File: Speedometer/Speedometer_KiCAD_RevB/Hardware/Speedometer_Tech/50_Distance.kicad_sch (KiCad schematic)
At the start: 30 parts, among them U510 TLC59108IPWR, U511 TLC59108IPWR, U512 TLC59108IPWR, U513 TLC59108IPWR, U514 TLC59108IPWR, U515 TLC59108IPWR, U520 TLC59108IPWR, U521 TLC59108IPWR, U522 TLC59108IPWR, U523 TLC59108IPWR

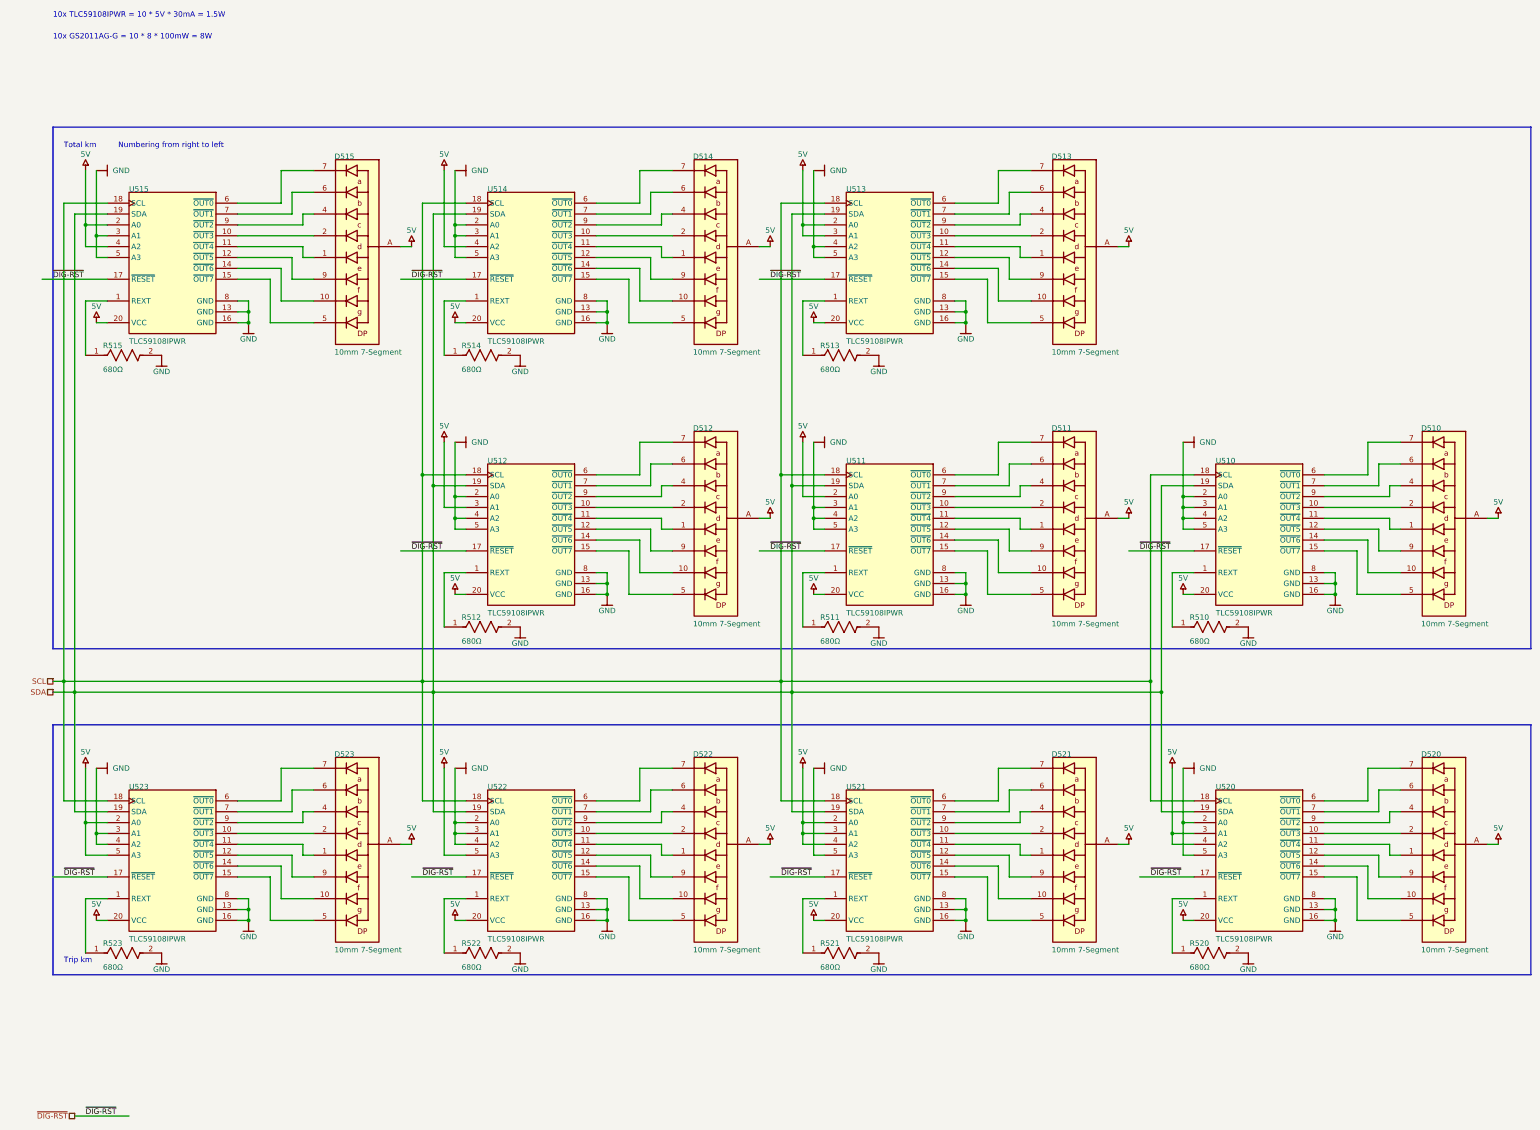
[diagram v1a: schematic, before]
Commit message: Speedometer DRC mostly passed
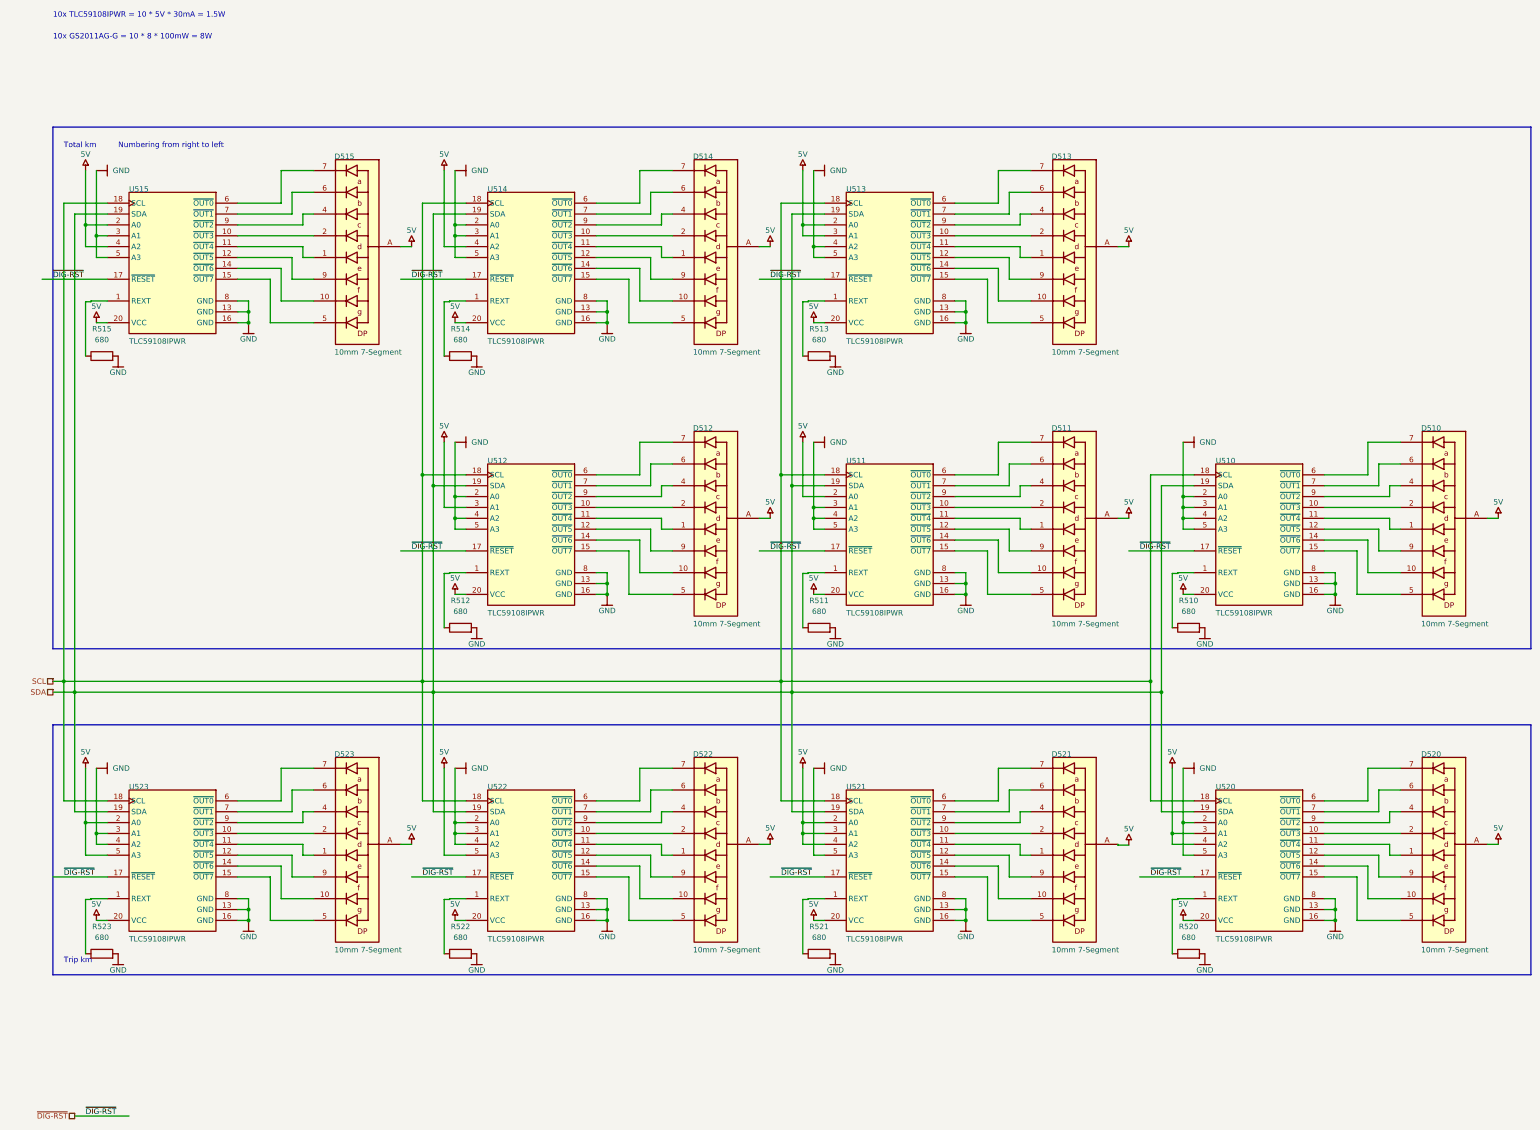
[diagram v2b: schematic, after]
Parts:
- removed R510, R511, R512, R513, R514, R515, R520, R521, R522, R523: 680Ω, FP-CRCW0603-e3-IPC_A, symbol Speedometer_Tech-altium-import:Designator_0_1029c3af85768c4190bb7ad29bc67b5
- added R510, R511, R512, R513, R514, R515, R520, R521, R522, R523: 680, Resistor_SMD:R_0603_1608Metric, symbol Device:R
- U510, U511, U512, U513, U514, U515, U520, U521, U522, U523: footprint PW0020A_M -> Package_SO:TSSOP-20_4.4x6.5mm_P0.65mm
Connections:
- net GND: now also R510.2, R511.2, R512.2, R513.2, R514.2, R515.2, R520.2, R521.2, R522.2, R523.2
- net at U520.1 (REXT): now also R520.1
- net at U515.1 (REXT): now also R515.1
- net at U522.1 (REXT): now also R522.1
- net at U521.1 (REXT): now also R521.1
- net at U523.1 (REXT): now also R523.1
- net at U511.1 (REXT): now also R511.1
- net at U510.1 (REXT): now also R510.1
- net at U513.1 (REXT): now also R513.1
- net at U514.1 (REXT): now also R514.1
- net at U512.1 (REXT): now also R512.1
